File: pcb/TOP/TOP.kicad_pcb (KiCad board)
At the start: 2 copper layers, 52 x 63 mm, 15 parts, among them J1 Conn_01x04

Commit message: [All] Flip board to board connector on upper PCB (obstructed some silk)
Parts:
- added C1: 100uF, Capacitor_THT:CP_Radial_D5.0mm_P2.00mm, F.Cu at (75.8, 82.5)
- added C100: 100uF, Capacitor_THT:CP_Radial_D5.0mm_P2.00mm, F.Cu at (61.9, 91.0)
- added C101: 10uF, Capacitor_SMD:C_0805_2012Metric, F.Cu at (80.6, 87.2)
- added C102: 220nF, Capacitor_SMD:C_0603_1608Metric, F.Cu at (96.9, 83.0)
- added C13: 10uF, Capacitor_SMD:C_0805_2012Metric, F.Cu at (61.8, 99.1)
- added C14: 10uF, Capacitor_SMD:C_0805_2012Metric, F.Cu at (74.6, 91.7)
- added C2: 10uF, Capacitor_SMD:C_0805_2012Metric, F.Cu at (87.2, 80.7)
- added C3: 10uF, Capacitor_SMD:C_0805_2012Metric, F.Cu at (68.4, 95.2)
- added C5: 22uF, Capacitor_SMD:C_1206_3216Metric, F.Cu at (62.4, 95.9)
- added C9: 10uF, Capacitor_SMD:C_0805_2012Metric, F.Cu at (67.4, 98.3)
- added D1: 1N4004, Diode_THT:D_DO-41_SOD81_P10.16mm_Horizontal, F.Cu at (61.4, 81.3)
- added D2: 1N4004, Diode_THT:D_DO-41_SOD81_P10.16mm_Horizontal, F.Cu at (61.4, 85.6)
- added JP100: Jmp, Jumper:SolderJumper-2_P1.3mm_Open_TrianglePad1.0x1.5mm, F.Cu at (72.8, 95.5)
- added Q1: BF545A, Package_TO_SOT_SMD:SOT-23, F.Cu at (75.9, 88.0)
- added Q2: BF545A, Package_TO_SOT_SMD:SOT-23, F.Cu at (82.6, 81.4)
- added R10: 2k2, Resistor_SMD:R_0603_1608Metric, F.Cu at (92.8, 89.5)
- added R100: 1M, Resistor_SMD:R_0603_1608Metric, F.Cu at (81.1, 95.5)
- added R101: 2M2, Resistor_SMD:R_0603_1608Metric, F.Cu at (82.9, 91.5)
- added R102: 390R, Resistor_SMD:R_0603_1608Metric, F.Cu at (75.7, 99.5)
- added R103: 2k2, Resistor_SMD:R_0603_1608Metric, F.Cu at (88.9, 84.5)
- added R15: 10K, Resistor_SMD:R_0603_1608Metric, F.Cu at (88.8, 89.5)
- added R16: 10K, Resistor_SMD:R_0603_1608Metric, F.Cu at (92.9, 84.5)
- added R2: 1M, Resistor_SMD:R_0603_1608Metric, F.Cu at (88.9, 87.0)
- added R3: 10K, Resistor_SMD:R_0603_1608Metric, F.Cu at (81.1, 98.0)
- added R4: 10K, Resistor_SMD:R_0603_1608Metric, F.Cu at (85.1, 94.0)
- added R5: 10K, Resistor_SMD:R_0603_1608Metric, F.Cu at (84.8, 88.9)
- added R6: 10K, Resistor_SMD:R_0603_1608Metric, F.Cu at (95.5, 80.4)
- added R9: 10K, Resistor_SMD:R_0603_1608Metric, F.Cu at (92.9, 87.0)
- added TP1: TP, TestPoint:TestPoint_Pad_D2.0mm, F.Cu at (91.5, 81.2)
- added TP100: TP, TestPoint:TestPoint_Pad_D2.0mm, F.Cu at (78.8, 92.2)
- added TP2: TP, TestPoint:TestPoint_Pad_D2.0mm, F.Cu at (71.7, 99.3)
- added TP3: TP, TestPoint:TestPoint_Pad_D2.0mm, F.Cu at (77.0, 96.3)
- added TP4: TP, TestPoint:TestPoint_Pad_D2.0mm, F.Cu at (84.8, 85.7)
- added U2: L78L15_SOT89, Package_TO_SOT_SMD:SOT-89-3, F.Cu at (69.3, 90.7)
- moved J1 7.57 mm to (153.2, 128.0), turned to 180 degrees
- renumbered RV102 to RV1
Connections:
- J1 pad 1: GND -> Upper_PCB_Input
- J1 pad 2: +9V -> Upper_PCB_Output
- J1 pad 3: Upper_PCB_Output -> +9V
- J1 pad 4: Upper_PCB_Input -> GND
- RV1 pad 1: unconnected-(RV102-Pad1) -> Net-(RV1-Pad1)
- RV1 pad 2: unconnected-(RV102-Pad2) -> Net-(RV1-Pad2)
- RV1 pad 3: unconnected-(RV102-Pad3) -> Net-(RV1-Pad3)

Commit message: [TOP] Continue schematic
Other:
- board text added: "Gain"
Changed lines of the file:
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@@
     (effects (font (size 1.5 1.5) (thickness 0.3)) (justify mirror))
   )
-  (gr_text "Pot" (at 166.7 84) (layer "B.SilkS")
+  (gr_text "Gain" (at 166.7 84) (layer "B.SilkS")
     (effects (font (size 1.5 1.5) (thickness 0.3)) (justify mirror))
   )
@@
     (effects (font (size 0.7 0.7) (thickness 0.13)))
   )
-  (gr_text "Pot" (at 166.5 77.3) (layer "F.SilkS")
+  (gr_text "Gain" (at 166.5 77.3) (layer "F.SilkS")
     (effects (font (size 1.5 1.5) (thickness 0.3)))
   )

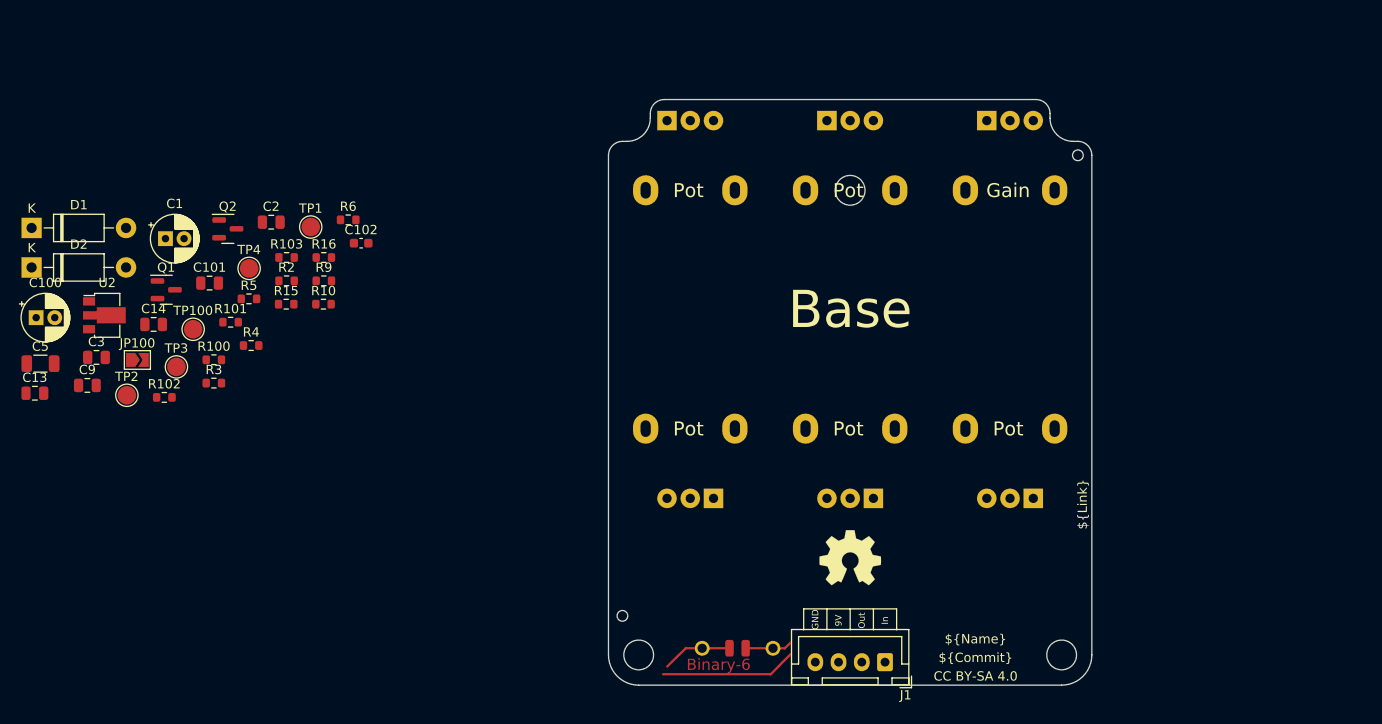
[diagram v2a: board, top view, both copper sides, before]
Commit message: [TOP] Consolidate footprints; Add bypass cap to U1
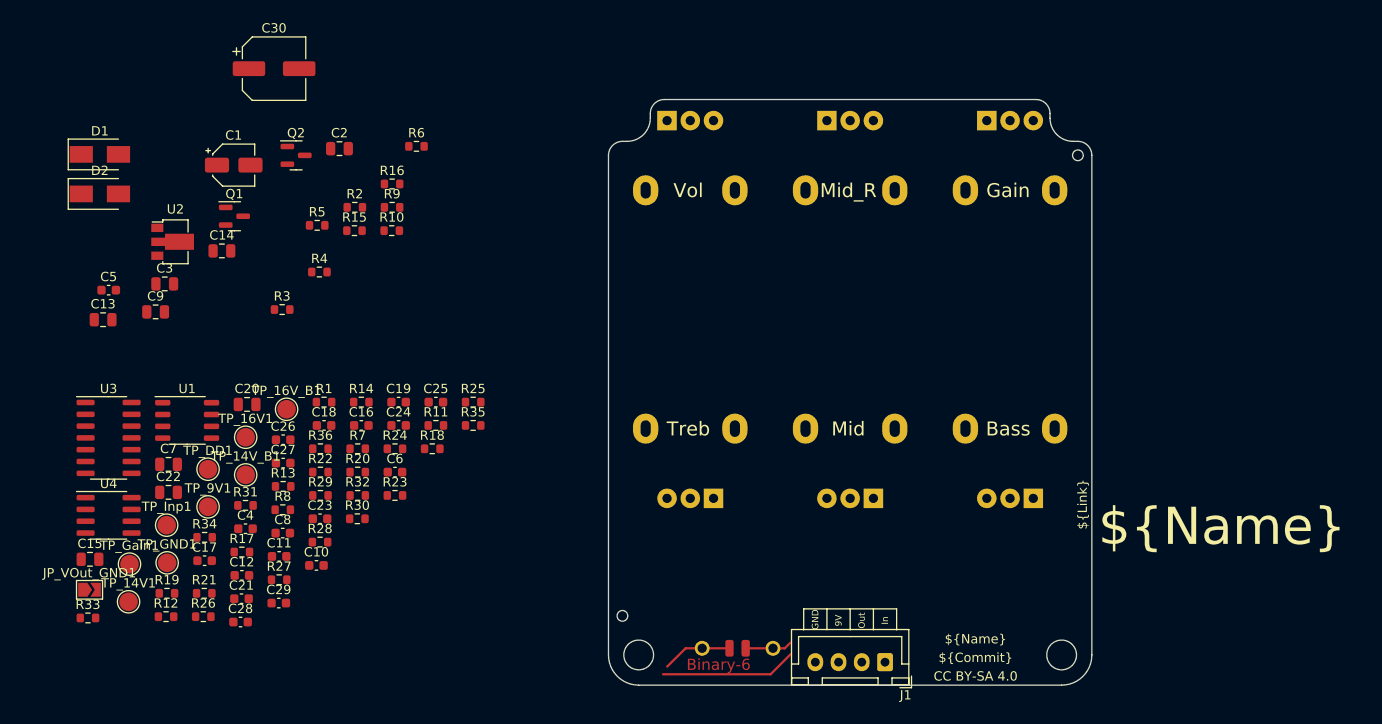
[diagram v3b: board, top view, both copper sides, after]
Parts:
- removed C100: 100uF, Capacitor_THT:CP_Radial_D5.0mm_P2.00mm
- removed C101: 10uF, Capacitor_SMD:C_0805_2012Metric
- removed C102: 220nF, Capacitor_SMD:C_0603_1608Metric
- removed JP100: Jmp, Jumper:SolderJumper-2_P1.3mm_Open_TrianglePad1.0x1.5mm
- removed the MK2 at (149.5, 77.3)
- removed R100: 1M, Resistor_SMD:R_0603_1608Metric
- removed R101: 2M2, Resistor_SMD:R_0603_1608Metric
- removed R102: 390R, Resistor_SMD:R_0603_1608Metric
- removed R103: 2k2, Resistor_SMD:R_0603_1608Metric
- removed the REF** at (149.5, 116.8) (x2)
- removed TP1, TP100, TP2, TP3, TP4: TP, TestPoint:TestPoint_Pad_D2.0mm
- added C10: 220nF, Capacitor_SMD:C_0603_1608Metric, F.Cu at (92.1, 117.6)
- added C11: 100pF, Capacitor_SMD:C_0603_1608Metric, F.Cu at (88.1, 116.7)
- added C12: 100nF, Capacitor_SMD:C_0603_1608Metric, F.Cu at (84.1, 118.7)
- added C15: 10nF, Capacitor_SMD:C_0805_2012Metric, F.Cu at (67.7, 117.0)
- added C16: 220nF, Capacitor_SMD:C_0603_1608Metric, F.Cu at (96.9, 102.6)
- added C17: 47nF, Capacitor_SMD:C_0603_1608Metric, F.Cu at (80.1, 117.1)
- added C18: 1nF, Capacitor_SMD:C_0603_1608Metric, F.Cu at (92.9, 102.6)
- added C19: 470nF, Capacitor_SMD:C_0603_1608Metric, F.Cu at (100.9, 100.1)
- added C20: 10uF, Capacitor_SMD:C_0805_2012Metric, F.Cu at (84.6, 100.3)
- added C21: 22nF, Capacitor_SMD:C_0603_1608Metric, F.Cu at (84.0, 121.2)
- added C22: 10uF, Capacitor_SMD:C_0805_2012Metric, F.Cu at (76.2, 109.8)
- added C23: 22nF, Capacitor_SMD:C_0603_1608Metric, F.Cu at (92.5, 112.6)
- added C24: 22nF, Capacitor_SMD:C_0603_1608Metric, F.Cu at (100.9, 102.6)
- added C25: 220nF, Capacitor_SMD:C_0603_1608Metric, F.Cu at (104.9, 100.1)
- added C26: 68nF, Capacitor_SMD:C_0603_1608Metric, F.Cu at (88.5, 104.1)
- added C27: 1nF, Capacitor_SMD:C_0603_1608Metric, F.Cu at (88.5, 106.6)
- added C28: 470nF, Capacitor_SMD:C_0603_1608Metric, F.Cu at (83.9, 123.7)
- added C29: 1nF, Capacitor_SMD:C_0603_1608Metric, F.Cu at (88.0, 121.7)
- added C30: 100uF, Capacitor_SMD:CP_Elec_6.3x5.4_Nichicon, F.Cu at (87.5, 64.2)
- added C4: 22nF, Capacitor_SMD:C_0603_1608Metric, F.Cu at (84.5, 113.7)
- added C6: 2.2uF, Capacitor_SMD:C_0603_1608Metric, F.Cu at (100.5, 107.6)
- added C7: 10nF, Capacitor_SMD:C_0805_2012Metric, F.Cu at (76.2, 106.8)
- added C8: 220nF, Capacitor_SMD:C_0603_1608Metric, F.Cu at (88.5, 114.1)
- added JP_VOut_GND1: Jmp, Jumper:SolderJumper-2_P1.3mm_Open_TrianglePad1.0x1.5mm, F.Cu at (67.7, 120.2)
- added R1: 51R, Resistor_SMD:R_0603_1608Metric, F.Cu at (92.9, 100.1)
- added R11: 22K, Resistor_SMD:R_0603_1608Metric, F.Cu at (104.9, 102.6)
- added R12: 100K, Resistor_SMD:R_0603_1608Metric, F.Cu at (75.9, 123.1)
- added R13: 1K, Resistor_SMD:R_0603_1608Metric, F.Cu at (88.5, 109.1)
- added R14: 7K5, Resistor_SMD:R_0603_1608Metric, F.Cu at (96.9, 100.1)
- added R17: 15K, Resistor_SMD:R_0603_1608Metric, F.Cu at (84.1, 116.2)
- added R18: 10K, Resistor_SMD:R_0603_1608Metric, F.Cu at (104.5, 105.1)
- added R19: 47K, Resistor_SMD:R_0603_1608Metric, F.Cu at (76.0, 120.6)
- added R20: 47K, Resistor_SMD:R_0603_1608Metric, F.Cu at (96.5, 107.6)
- added R21: 47K, Resistor_SMD:R_0603_1608Metric, F.Cu at (80.0, 120.6)
- added R22: 39K, Resistor_SMD:R_0603_1608Metric, F.Cu at (92.5, 107.6)
- added R23: 1K, Resistor_SMD:R_0603_1608Metric, F.Cu at (100.5, 110.1)
- added R24: 1M, Resistor_SMD:R_0603_1608Metric, F.Cu at (100.5, 105.1)
- added R25: 10K, Resistor_SMD:R_0603_1608Metric, F.Cu at (108.9, 100.1)
- added R26: 10K, Resistor_SMD:R_0603_1608Metric, F.Cu at (79.9, 123.1)
- added R27: 10K, Resistor_SMD:R_0603_1608Metric, F.Cu at (88.1, 119.2)
- added R28: 2K2, Resistor_SMD:R_0603_1608Metric, F.Cu at (92.5, 115.1)
- added R29: 7K5, Resistor_SMD:R_0603_1608Metric, F.Cu at (92.5, 110.1)
- added R30: 470R, Resistor_SMD:R_0603_1608Metric, F.Cu at (96.5, 112.6)
- added R31: 10K, Resistor_SMD:R_0603_1608Metric, F.Cu at (84.5, 111.2)
- added R32: 1K, Resistor_SMD:R_0603_1608Metric, F.Cu at (96.5, 110.1)
- added R33: 10K, Resistor_SMD:R_0603_1608Metric, F.Cu at (67.5, 123.3)
- added R34: 330R, Resistor_SMD:R_0603_1608Metric, F.Cu at (80.1, 114.6)
- added R35: 470K, Resistor_SMD:R_0603_1608Metric, F.Cu at (108.9, 102.6)
- added R36: 10K, Resistor_SMD:R_0603_1608Metric, F.Cu at (92.5, 105.1)
- added R7: 470K, Resistor_SMD:R_0603_1608Metric, F.Cu at (96.5, 105.1)
- added R8: 470K, Resistor_SMD:R_0603_1608Metric, F.Cu at (88.5, 111.6)
- added TP_14V1: TP, TestPoint:TestPoint_Pad_D2.0mm, F.Cu at (71.9, 121.5)
- added TP_14V_B1: TP, TestPoint:TestPoint_Pad_D2.0mm, F.Cu at (84.5, 107.9)
- added TP_16V1: TP, TestPoint:TestPoint_Pad_D2.0mm, F.Cu at (84.5, 103.8)
- added TP_16V_B1: TP, TestPoint:TestPoint_Pad_D2.0mm, F.Cu at (88.9, 100.8)
- added TP_9V1: TP, TestPoint:TestPoint_Pad_D2.0mm, F.Cu at (80.4, 111.3)
- added TP_DD1: TP, TestPoint:TestPoint_Pad_D2.0mm, F.Cu at (80.4, 107.3)
- added TP_GND1: TP, TestPoint:TestPoint_Pad_D2.0mm, F.Cu at (76.0, 117.3)
- added TP_Gain1: TP, TestPoint:TestPoint_Pad_D2.0mm, F.Cu at (72.0, 117.5)
- added TP_Inp1: TP, TestPoint:TestPoint_Pad_D2.0mm, F.Cu at (76.0, 113.3)
- added U1: ICL7660, Package_SO:SOP-8_3.9x4.9mm_P1.27mm, F.Cu at (78.2, 102.0)
- added U3: TL074, Package_SO:SOIC-14_3.9x8.7mm_P1.27mm, F.Cu at (69.7, 103.9)
- added U4: OPA2604, Package_SO:SOIC-8_3.9x4.9mm_P1.27mm, F.Cu at (69.7, 112.2)
- C1: value 100uF -> 10uF; footprint Capacitor_THT:CP_Radial_D5.0mm_P2.00mm -> Capacitor_SMD:CP_Elec_4x5.4
- C5: value 22uF -> 470pF; footprint Capacitor_SMD:C_1206_3216Metric -> Capacitor_SMD:C_0603_1608Metric
- D1, D2: footprint Diode_THT:D_DO-41_SOD81_P10.16mm_Horizontal -> Diode_SMD:D_SMA
- R10: value 2k2 -> 2K2
- R4: value 10K -> 1M
- RV2: renamed from RV101; value 100K Lin -> 1M lin
- RV3: renamed from RV100; value 100K Lin -> 100K Log
- RV4: renamed from RV202; value 100K Lin -> 10k Lin
- RV5: renamed from RV201; value 100K Lin -> 25k Lin
- RV6: renamed from RV200; value 100K Lin -> 25k Lin
- moved C14 10.8 mm to (81.9, 83.8)
- moved C3 10.8 mm to (75.8, 87.3)
- moved C5 10.8 mm to (69.7, 88.0)
- moved Q2 10.8 mm to (89.9, 73.5)
- moved R16 10.8 mm to (100.2, 76.6)
- moved R5 10.8 mm to (92.2, 81.0)
- moved C13 10.8 mm to (69.1, 91.2)
- moved C1 10.8 mm to (83.2, 74.6)
- moved C2 10.8 mm to (94.6, 72.8)
- moved C9 10.8 mm to (74.8, 90.3)
- moved D1 10.8 mm to (68.8, 73.4)
- moved D2 10.8 mm to (68.8, 77.7)
- moved Q1 10.8 mm to (83.3, 80.1)
- moved R10 10.8 mm to (100.2, 81.6)
- moved R15 10.8 mm to (96.2, 81.6)
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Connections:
- C5 pad 1: unconnected-(C5-Pad1) -> Net-(C15-Pad2)
- C5 pad 2: unconnected-(C5-Pad2) -> Net-(C5-Pad2)
- R4 pad 1: unconnected-(R4-Pad1) -> Net-(C5-Pad2)
- R4 pad 2: unconnected-(R4-Pad2) -> Net-(C15-Pad2)
- RV2 pad 1: unconnected-(RV101-Pad1) -> Net-(R31-Pad1)
- RV2 pad 2: unconnected-(RV101-Pad2) -> Net-(C20-Pad1)
- RV2 pad 3: unconnected-(RV101-Pad3) -> Net-(C20-Pad1)
- RV3 pad 1: unconnected-(RV100-Pad1) -> Net-(R21-Pad2)
- RV3 pad 2: unconnected-(RV100-Pad2) -> Net-(C19-Pad2)
- RV3 pad 3: unconnected-(RV100-Pad3) -> GND
- RV4 pad 1: unconnected-(RV202-Pad1) -> Net-(R33-Pad1)
- RV4 pad 2: unconnected-(RV202-Pad2) -> Net-(C25-Pad2)
- RV4 pad 3: unconnected-(RV202-Pad3) -> Net-(R32-Pad2)
- RV5 pad 1: unconnected-(RV201-Pad1) -> Net-(R27-Pad2)
- RV5 pad 2: unconnected-(RV201-Pad2) -> Net-(C23-Pad2)
- RV5 pad 3: unconnected-(RV201-Pad3) -> Net-(C27-Pad2)
- RV6 pad 1: unconnected-(RV200-Pad1) -> Net-(R27-Pad2)
- RV6 pad 2: unconnected-(RV200-Pad2) -> Net-(C21-Pad1)
- RV6 pad 3: unconnected-(RV200-Pad3) -> Net-(C27-Pad2)
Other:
- board text added: "Bass"
- board text added: "Mid"
- board text added: "Mid_R"
- board text added: "Midrange"
- board text added: "Treb"
- board text added: "Treble"
- board text added: "Vol"
- board text added: "Volume"
- board text removed: "Base"
- board text removed: "Either delete mounting hole or pot"
- board text removed: "Pot"

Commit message: [TOP] Route power, input and gain stages
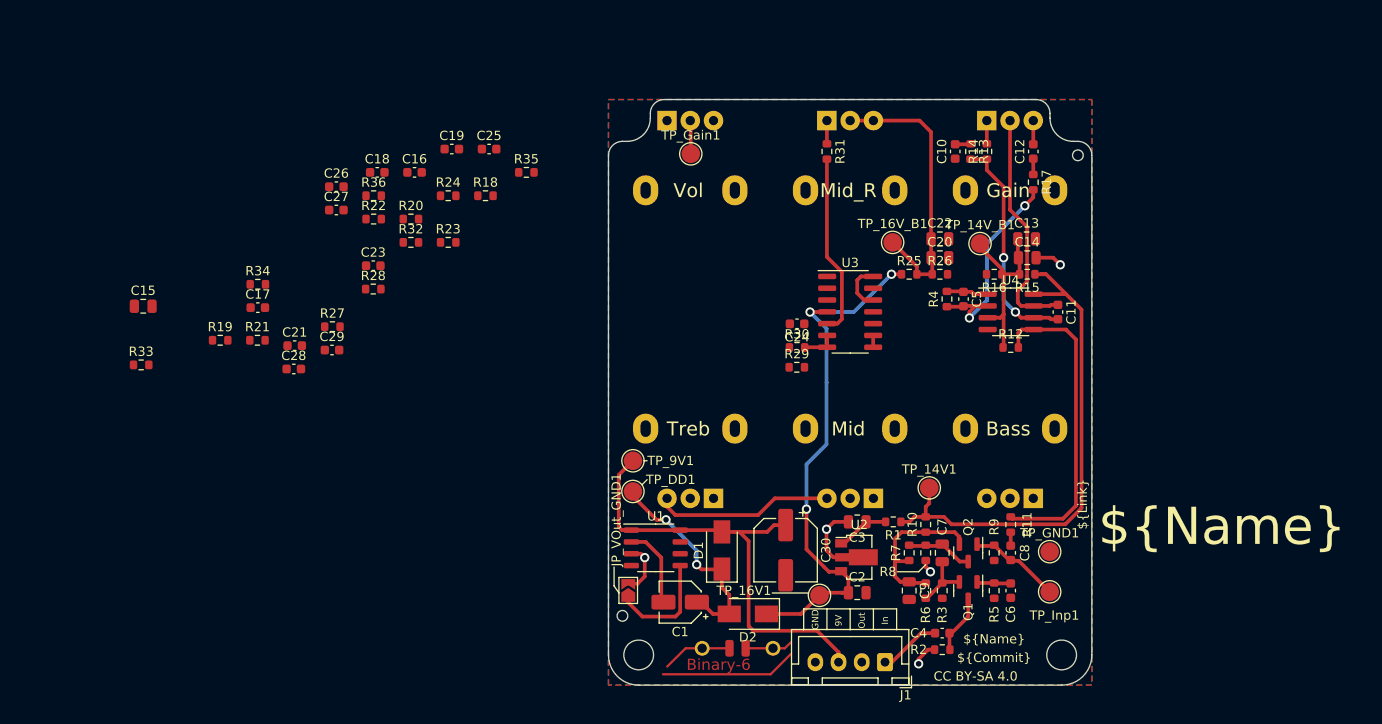
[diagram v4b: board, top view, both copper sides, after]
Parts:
- moved C13 99.7 mm to (168.5, 82.5)
- moved U4 99.5 mm to (166.8, 90.3)
- moved C12 96.6 mm to (169.2, 73.1), turned to 90 degrees
- moved R12 95.4 mm to (166.8, 94.2)
- moved TP_Inp1 95.3 mm to (171.0, 120.5)
- moved TP_GND1 94.9 mm to (171.0, 116.1)
- moved R17 94.0 mm to (169.2, 76.4), turned to -90 degrees
- moved C5 92.0 mm to (161.7, 89.0), turned to -90 degrees
- moved Q1 88.6 mm to (162.2, 120.3), turned to -90 degrees
- moved C11 87.8 mm to (171.9, 90.4), turned to -90 degrees
- moved R26 87.4 mm to (159.2, 86.3)
- moved C22 87.3 mm to (159.2, 82.5)
- moved TP_14V1 87.0 mm to (158.0, 109.3)
- moved C14 86.6 mm to (168.6, 84.5)
- moved C9 86.4 mm to (155.8, 120.3), turned to -90 degrees
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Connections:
- C16 pad 1: Net-(C16-Pad1) -> Net-(C15-Pad2)
- C16 pad 2: Net-(C15-Pad2) -> Net-(C16-Pad2)
- C2 pad 1: +4V5 -> +16V
- D2 pad 1: +4V5 -> +16V
- R1 pad 1: +4V5 -> +14V
- R10 pad 2: +4V5 -> +14V
- R15 pad 1: +4V5 -> +14V
- R18 pad 1: Net-(C16-Pad1) -> Net-(C16-Pad2)
- R23 pad 2: Net-(R23-Pad2) -> Net-(U3-Pad13)
- R24 pad 2: Net-(R23-Pad2) -> Net-(U3-Pad13)
- R25 pad 1: +4V5 -> +16V
- R27 pad 2: Net-(R27-Pad2) -> Net-(U3-Pad2)
- R33 pad 2: Net-(R27-Pad2) -> Net-(U3-Pad2)
- RV5 pad 1: Net-(R27-Pad2) -> Net-(U3-Pad2)
- RV6 pad 1: Net-(R27-Pad2) -> Net-(U3-Pad2)
- TP_14V1 pad 1: +4V5 -> +14V
- TP_16V1 pad 1: +4V5 -> +16V
- U2 pad 3: +4V5 -> +16V
- U3 pad 1: Net-(R27-Pad1) -> Net-(C27-Pad1)
- U3 pad 12: Net-(R27-Pad2) -> Net-(R27-Pad1)
- U3 pad 13: Net-(C27-Pad2) -> Net-(U3-Pad13)
- U3 pad 14: Net-(C27-Pad1) -> Net-(R27-Pad1)
- U3 pad 2: Net-(R27-Pad1) -> Net-(U3-Pad2)
- U3 pad 3: Net-(R23-Pad2) -> Net-(C27-Pad2)
- U3 pad 4: +4V5 -> +16V
- U4 pad 8: +4V5 -> +14V
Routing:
- net +16V: track 0.00 -> 58.4 mm, vias 0 -> 3
- net +14V: track 0.00 -> 55.6 mm
- net +9V: track 0.00 -> 49.2 mm
- net Net-(R11-Pad2): track 0.00 -> 33.9 mm
- net Net-(C20-Pad1): track 0.00 -> 30.9 mm
- net Net-(C11-Pad1): track 0.00 -> 25.3 mm
- net Net-(C11-Pad2): track 0.00 -> 24.4 mm, vias 0 -> 2
- net Net-(C1-Pad1): track 0.00 -> 23.4 mm, vias 0 -> 2
- net Net-(C5-Pad2): track 0.00 -> 22.6 mm, vias 0 -> 2
- net Net-(C13-Pad1): track 0.00 -> 20.0 mm
- net Net-(C24-Pad1): track 0.00 -> 19.7 mm
- net GND: track 0.00 -> 19.6 mm, vias 0 -> 5
- net Net-(C27-Pad2): track 0.00 -> 19.2 mm
- net Net-(C9-Pad1): track 0.00 -> 18.3 mm
- net Net-(JP_VOut_GND1-Pad1): track 0.00 -> 12.0 mm
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- added copper zone on B.Cu, net GND
- added copper zone on F.Cu, net GND

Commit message: [TOP] Finish initial PCB design
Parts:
- removed TP_Gain1: TP, TestPoint:TestPoint_Pad_D2.0mm
- moved R33 96.6 mm to (169.2, 107.3), turned to 90 degrees
- moved R34 69.8 mm to (155.2, 94.2), turned to 180 degrees
- moved R32 66.6 mm to (164.2, 107.3), turned to -90 degrees
- moved C25 65.8 mm to (166.7, 107.3), turned to -90 degrees
- moved C26 62.9 mm to (155.2, 92.4)
- moved C15 62.3 mm to (135.7, 92.6)
- moved R27 56.3 mm to (149.6, 84.4), turned to 180 degrees
- moved C28 52.1 mm to (141.0, 87.4), turned to 90 degrees
- moved C17 50.0 mm to (135.7, 86.4)
- moved C27 49.2 mm to (142.8, 87.4), turned to -90 degrees
- moved R19 47.3 mm to (129.1, 92.6), turned to 180 degrees
- moved R36 47.3 mm to (144.5, 87.4), turned to 90 degrees
- moved C23 47.2 mm to (143.8, 97.7), turned to 180 degrees
- moved C21 44.6 mm to (132.3, 107.3), turned to 90 degrees
- moved R21 43.9 mm to (129.1, 86.4), turned to 180 degrees
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- renumbered TP_14V1 to 14V1, TP_14V_B1 to 14V_B1, TP_16V1 to 16V1, TP_16V_B1 to 16V_B1, TP_9V1 to 9V1, TP_DD1 to DD1, TP_GND1 to GND1, TP_Inp1 to Inp1, JP_VOut_GND1 to VOut-GND1
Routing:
- net Net-(U3-Pad2): track 0.00 -> 73.3 mm, vias 0 -> 3
- net Net-(C27-Pad2): track 19.2 -> 75.4 mm
- net Upper_PCB_Output: track 0.00 -> 44.2 mm, vias 0 -> 1
- net Net-(C15-Pad2): track 4.51 -> 45.0 mm, vias 0 -> 2
- net Net-(U3-Pad13): track 0.00 -> 29.0 mm, vias 0 -> 2
- net Net-(C25-Pad1): track 0.00 -> 24.7 mm, vias 0 -> 2
- net Net-(R21-Pad2): track 0.00 -> 19.6 mm
- net GND: track 19.6 -> 37.1 mm, vias 5 -> 19
- net Net-(C23-Pad2): track 0.00 -> 17.1 mm
- net Net-(C17-Pad2): track 0.00 -> 14.0 mm
- net Net-(C20-Pad1): track 30.9 -> 40.0 mm
- net Net-(R19-Pad2): track 0.00 -> 8.68 mm
- net Net-(C18-Pad1): track 0.00 -> 7.70 mm, vias 0 -> 2
- net Net-(C27-Pad1): track 0.00 -> 6.09 mm
- net Net-(C15-Pad1): track 0.00 -> 4.83 mm
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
